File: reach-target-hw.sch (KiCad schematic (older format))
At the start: 53 parts, among them J1 CONN_01X02, J2 CONN_01X02, J3 CONN_02X05, J4 MODULE_HEADER, J5 MODULE_HEADER, J6 MODULE_HEADER, P1 CONN_01X05, P2 CONN_01X05, P3 CONN_01X02, P4 CONN_01X02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

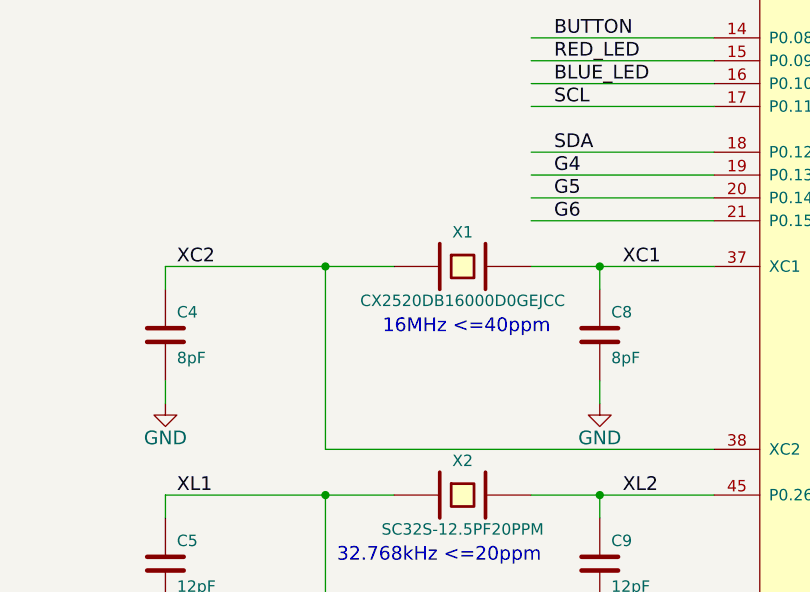
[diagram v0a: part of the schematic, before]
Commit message: symbol swap for 4pin xtal
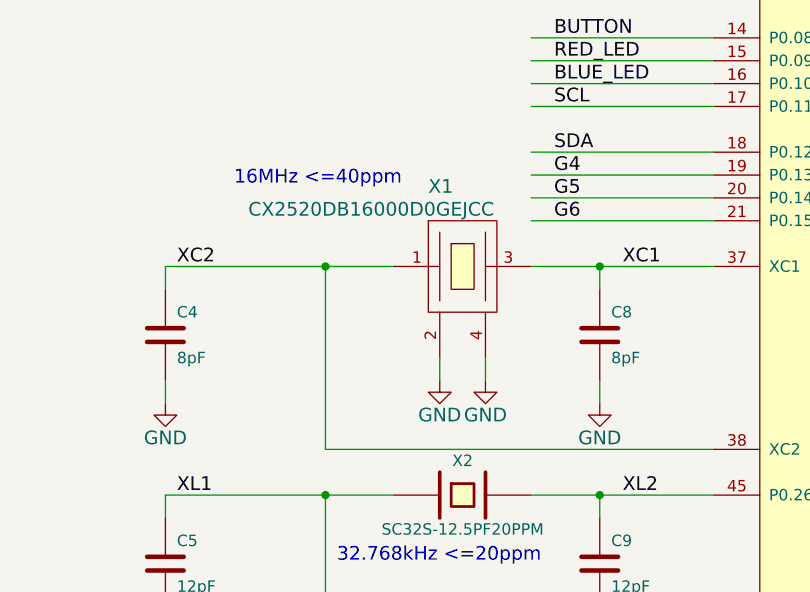
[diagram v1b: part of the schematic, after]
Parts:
- removed X1: CX2520DB16000D0GEJCC, !Parts:CX2520DB, symbol CRYSTAL
- added X1: CX2520DB16000D0GEJCC, symbol CRYSTAL-4
- J5, J6: footprint !Parts:MODULE_HEADER_TESSEL -> Pin_Headers:Pin_Header_Straight_1x10
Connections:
- wire segments 216 -> 218

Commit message: forgot to connect the eeprom
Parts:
- added R10, R11: 0R DNP, !Parts:SMD-0402, symbol R
- X1: footprint (none) -> !Parts:CX2520DB
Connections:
- net labels added: ANT, ANT1, ANT2, BLED, PI, RLED, VDD_PA
- wire segments 218 -> 222
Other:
- moved on the sheet: U1

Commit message: preliminary placement, i2c pull resistors
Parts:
- added R? (x2): 10kR DNP, !Parts:SMD-0402, symbol R
- C2, C3: footprint !Parts:SMD-0603 -> !Parts:SMD-0402
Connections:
- wire segments 222 -> 266
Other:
- moved on the sheet: R10, R11, U1

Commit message: never thought fitting all the io breakout would be the hard part of this board...
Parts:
- gave numbers to parts that had none: 2
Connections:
- net labels added: SWDIO-~RESET
- wire segments 266 -> 226
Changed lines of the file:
@@
 $EndComp
 Text Label 6800 2900 0    60   ~ 0
-SWDIO/~RESET
+SWDIO-~RESET
 Text Label 6800 3000 0    60   ~ 0
 SWDCLK
@@
 $EndComp
 Text Label 9400 9000 2    60   ~ 0
-SWDIO/~RESET
+SWDIO-~RESET
 Text Label 9400 9100 2    60   ~ 0
 SWDCLK
@@
 	2900 2800 2900 2900
 Wire Wire Line
-	2200 2800 2300 2800
-Wire Wire Line
-	2300 2800 2900 2800
-Wire Wire Line
-	2900 2800 3100 2800
+	2200 2800 3100 2800
 Wire Wire Line
 	2600 2300 2600 2200
@@
 	2600 1700 2600 1800
 Wire Wire Line
-	1500 1700 1700 1700
-Wire Wire Line
-	1700 1700 2200 1700
-Wire Wire Line
-	2200 1700 2600 1700
-Wire Wire Line
-	2600 1700 3000 1700
+	1500 1700 3000 1700
 Wire Wire Line
 	3000 2400 3800 2400
@@
 	5300 2800 5200 2800
 Wire Wire Line
-	5300 2700 5300 2800
-Wire Wire Line
-	5300 2800 5300 3000
+	5300 2700 5300 3000
 Wire Wire Line
 	5200 2700 5300 2700
 Wire Wire Line
-	5200 2400 5600 2400
-Wire Wire Line
-	5600 2400 5700 2400
+	5200 2400 5700 2400
 Wire Wire Line
 	5700 2400 5700 2200
@@
 	12000 5100 12000 5200
 Wire Wire Line
-	11800 5100 12000 5100
-Wire Wire Line
-	12000 5100 12400 5100
+	11800 5100 12400 5100
 Connection ~ 11000 5100
 Wire Wire Line
@@
 	11000 5100 11000 5200
 Wire Wire Line
-	10800 5100 11000 5100
-Wire Wire Line
-	11000 5100 11200 5100
+	10800 5100 11200 5100
 Connection ~ 10200 5100
 Connection ~ 10100 6900
@@
 	10200 5100 10200 5200
 Wire Wire Line
-	9900 5100 10200 5100
-Wire Wire Line
-	10200 5100 10400 5100
-Wire Wire Line
-	10100 6800 10100 6900
-Wire Wire Line
-	10100 6900 10100 7000
+	9900 5100 10400 5100
+Wire Wire Line
+	10100 6800 10100 7000
 Wire Wire Line
 	9900 6900 10100 6900
@@
 	10200 6000 10200 5800
 Wire Wire Line
-	9900 6000 10100 6000
-Wire Wire Line
-	10100 6000 10200 6000
+	9900 6000 10200 6000
 Connection ~ 8800 2300
 Wire Wire Line
@@
 	8800 2300 8700 2300
 Wire Wire Line
-	8800 1400 8800 2300
-Wire Wire Line
-	8800 2300 8800 2400
+	8800 1400 8800 2400
 Wire Wire Line
 	11100 1400 11100 1600
@@
 	11800 2900 11800 3000
 Wire Wire Line
-	11700 2900 11800 2900
-Wire Wire Line
-	11800 2900 12600 2900
+	11700 2900 12600 2900
 Wire Wire Line
 	10700 2900 11100 2900
@@
 	5100 6200 5100 6300
 Wire Wire Line
-	5100 6200 5800 6200
-Wire Wire Line
-	5800 6200 6100 6200
+	5100 6200 6100 6200
 Wire Wire Line
 	5800 7000 5800 6200
@@
 	7000 6800 7000 6700
 Wire Wire Line
-	6700 6200 7000 6200
-Wire Wire Line
-	7000 6200 7500 6200
+	6700 6200 7500 6200
 Wire Wire Line
 	5100 5800 5100 5700
@@
 	5100 5200 5100 5300
 Wire Wire Line
-	5100 5200 5800 5200
-Wire Wire Line
-	5800 5200 6100 5200
+	5100 5200 6100 5200
 Wire Wire Line
 	5800 6000 5800 5200
@@
 	7000 5800 7000 5700
 Wire Wire Line
-	6700 5200 7000 5200
-Wire Wire Line
-	7000 5200 7500 5200
+	6700 5200 7500 5200
 Connection ~ 8400 2300
 Connection ~ 8500 2300
@@
 	8400 2300 8500 2300
 Wire Wire Line
-	8500 1450 8500 2300
-Wire Wire Line
-	8500 2300 8500 2400
+	8500 1450 8500 2400
 Wire Wire Line
 	6800 1450 8500 1450
 Wire Wire Line
-	6800 1150 6800 1450
-Wire Wire Line
-	6800 1450 6800 1600
+	6800 1150 6800 1600
 Wire Wire Line
 	6800 2100 6800 2000
@@
 	8400 1500 7600 1500
 Wire Wire Line
-	8400 1500 8400 2300
-Wire Wire Line
-	8400 2300 8400 2400
+	8400 1500 8400 2400
 Wire Wire Line
 	7600 2100 7600 2000
@@
 Connection ~ 8500 7500
 Wire Wire Line
-	8500 7500 8600 7500
-Wire Wire Line
-	8600 7500 8700 7500
-Wire Wire Line
-	8700 7500 8900 7500
+	8500 7500 8900 7500
 Wire Wire Line
 	8600 7400 8600 7500
 Wire Wire Line
-	8500 7400 8500 7500
-Wire Wire Line
-	8500 7500 8500 7600
+	8500 7400 8500 7600
 Wire Wire Line
 	3500 5200 2600 5200
 Wire Wire Line
-	3600 5300 3500 5300
-Wire Wire Line
-	3500 5300 2600 5300
+	2600 5300 3600 5300
 Wire Wire Line
 	3400 5500 2600 5500
@@
 	1700 7200 1700 7000
 Wire Wire Line
-	2400 7200 2600 7200
-Wire Wire Line
-	2600 7200 3000 7200
-Wire Wire Line
-	3000 7200 3700 7200
+	2400 7200 3700 7200
 Wire Wire Line
 	2600 7300 2600 7200
@@
 	7900 9000 9800 9000
 Wire Wire Line
-	7200 9100 7200 9200
-Wire Wire Line
-	7200 9200 7200 9500
+	7200 9100 7200 9500
 Wire Wire Line
 	7200 9200 7400 9200
@@
 	7400 9300 6700 9300
 Wire Wire Line
-	9800 8900 9800 9000
-Wire Wire Line
-	9800 9000 9800 9100
+	9800 8900 9800 9100
 Connection ~ 9800 9000
 Wire Wire Line
@@
 	1500 1800 1600 1800
 Wire Wire Line
-	1600 1800 1600 2400
-Wire Wire Line
-	1600 2400 1600 2600
+	1600 1800 1600 2600
 Wire Wire Line
 	1500 2400 1600 2400
@@
 	15100 6100 14700 6100
 Wire Wire Line
-	14700 6100 14700 6400
-Wire Wire Line
-	14700 6400 14700 7000
-Wire Wire Line
-	14700 7000 14700 7600
-Wire Wire Line
-	14700 7600 14700 8200
-Wire Wire Line
-	14700 8200 14700 8800
-Wire Wire Line
-	14700 8800 14700 9000
+	14700 6100 14700 9000
 Wire Wire Line
 	14800 8800 14700 8800
@@
 	15100 6200 14600 6200
 Wire Wire Line
-	14600 6000 14600 6200
-Wire Wire Line
-	14600 6200 14600 6500
-Wire Wire Line
-	14600 6500 14600 7100
-Wire Wire Line
-	14600 7100 14600 7700
-Wire Wire Line
-	14600 7700 14600 8300
-Wire Wire Line
-	14600 8300 14600 8900
+	14600 6000 14600 8900
 Wire Wire Line
 	14600 6500 14800 6500
@@
 RLED
 $Comp
-L R R?
+L R R13
 U 1 1 54D9731D
 P 4500 4750
-F 0 "R?" V 4580 4750 50  0000 C CNN
+F 0 "R13" V 4580 4750 50  0000 C CNN
 F 1 "10kR DNP" V 4507 4751 50  0000 C CNN
 F 2 "!Parts:SMD-0402" V 4430 4750 30  0001 C CNN
@@
 $EndComp
 $Comp
-L R R?
+L R R12
 U 1 1 54D975E9
 P 4200 4750
-F 0 "R?" V 4280 4750 50  0000 C CNN
+F 0 "R12" V 4280 4750 50  0000 C CNN
 F 1 "10kR DNP" V 4207 4751 50  0000 C CNN
 F 2 "!Parts:SMD-0402" V 4130 4750 30  0001 C CNN
@@
 	4200 5000 4200 5300
 $Comp
-L +3V3 #PWR?
+L +3V3 #PWR044
 U 1 1 54D977F4
 P 4500 4400
-F 0 "#PWR?" H 4500 4250 60  0001 C CNN
+F 0 "#PWR044" H 4500 4250 60  0001 C CNN
 F 1 "+3V3" H 4500 4540 60  0000 C CNN
 F 2 "" H 4500 4400 60  0000 C CNN
@@
 	4500 4500 4500 4400
 $Comp
-L +3V3 #PWR?
+L +3V3 #PWR045
 U 1 1 54D978E6
 P 4200 4400
-F 0 "#PWR?" H 4200 4250 60  0001 C CNN
+F 0 "#PWR045" H 4200 4250 60  0001 C CNN
 F 1 "+3V3" H 4200 4540 60  0000 C CNN
 F 2 "" H 4200 4400 60  0000 C CNN

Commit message: well there goes most of the layout...and the avdd return path :/
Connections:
- net labels removed: SWDIO/~RESET
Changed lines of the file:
@@
 $EndComp
 Text Label 9400 9400 2    60   ~ 0
-SWDIO/~RESET
+SWDIO-~RESET
 $Comp
 L R R7

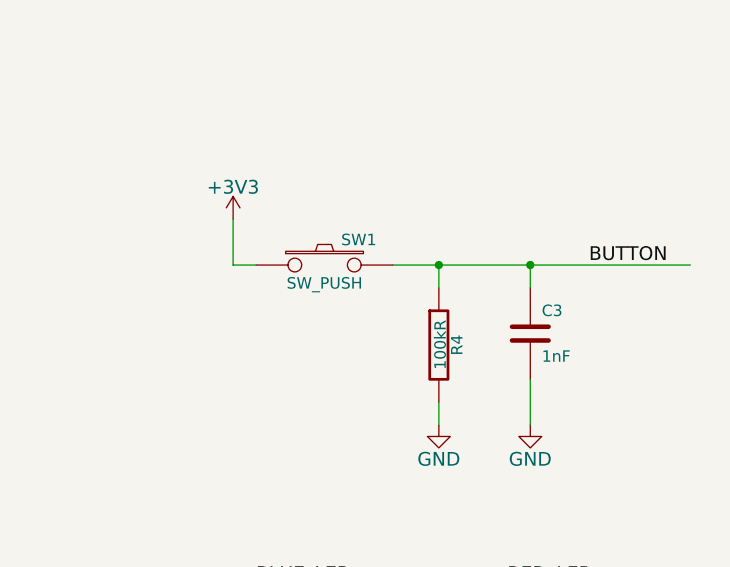
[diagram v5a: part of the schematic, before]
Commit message: swapped in real button
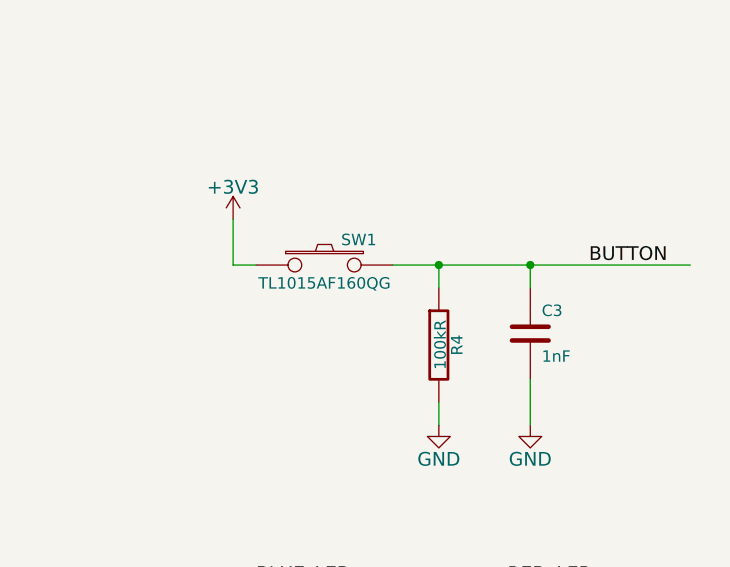
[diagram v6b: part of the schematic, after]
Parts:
- SW1: value SW_PUSH -> TL1015AF160QG; footprint Pin_Headers:Pin_Header_Straight_1x02 -> !Parts:TL1015AF160QG
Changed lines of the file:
@@
 P 2100 7200
 F 0 "SW1" H 2250 7310 50  0000 C CNN
-F 1 "SW_PUSH" H 2100 7120 50  0000 C CNN
-F 2 "Pin_Headers:Pin_Header_Straight_1x02" H 2100 7200 60  0001 C CNN
-F 3 "" H 2100 7200 60  0000 C CNN
+F 1 "TL1015AF160QG" H 2100 7120 50  0000 C CNN
+F 2 "!Parts:TL1015AF160QG" H 2100 7200 60  0001 C CNN
+F 3 "http://spec_sheets.e-switch.com/specs/P420000.pdf" H 2100 7200 60  0001 C CNN
 	1    2100 7200
 	1    0    0    -1

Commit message: better models
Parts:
- C1, C10, C17, C6: footprint !Parts:SMD-0603 -> !Parts:SMD-0603-C
- C11, C12, C13, C14, C15, C16, C18, C2, C3, C4, C5, C7, C8, C9: footprint !Parts:SMD-0402 -> !Parts:SMD-0402-C
- L1, L2, L4, L5, R1, R10, R11, R12, R13, R2, R3, R4, R5, R6, R7, R8, R9: footprint !Parts:SMD-0402 -> !Parts:SMD-0402-R
- L3: footprint !Parts:SMD-0603 -> !Parts:SMD-0603-R
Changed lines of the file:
@@
 F 0 "C10" H 7650 1900 50  0000 L CNN
 F 1 "4.7uF 10% X5R" H 7650 1700 50  0000 L CNN
-F 2 "!Parts:SMD-0603" H 7638 1650 30  0001 C CNN
+F 2 "!Parts:SMD-0603-C" H 7638 1650 30  0001 C CNN
 F 3 "" H 7600 1800 60  0000 C CNN
 	1    7600 1800
@@
 F 0 "L3" V 10350 2900 50  0000 C CNN
 F 1 "LBMF1608T100K" V 10500 2900 50  0000 C CNN
-F 2 "!Parts:SMD-0603" H 10400 2900 60  0001 C CNN
+F 2 "!Parts:SMD-0603-R" H 10400 2900 60  0001 C CNN
 F 3 "http://www.yuden.co.jp/ut/product/category/inductor/LBMF1608T100K.pdf" H 10400 2900 60  0001 C CNN
 	1    10400 2900
@@
 F 0 "C7" H 6850 1900 50  0000 L CNN
 F 1 "100nF 10% X7R" H 6850 1700 50  0000 L CNN
-F 2 "!Parts:SMD-0402" H 6838 1650 30  0001 C CNN
+F 2 "!Parts:SMD-0402-C" H 6838 1650 30  0001 C CNN
 F 3 "" H 6800 1800 60  0000 C CNN
 	1    6800 1800
@@
 F 0 "C8" H 7050 5600 50  0000 L CNN
 F 1 "8pF" H 7050 5400 50  0000 L CNN
-F 2 "!Parts:SMD-0402" H 7038 5350 30  0001 C CNN
+F 2 "!Parts:SMD-0402-C" H 7038 5350 30  0001 C CNN
 F 3 "" H 7000 5500 60  0000 C CNN
 	1    7000 5500
@@
 F 0 "L4" V 11350 2900 50  0000 C CNN
 F 1 "CW100505-15NJ" V 11500 2900 50  0000 C CNN
-F 2 "!Parts:SMD-0402" H 11400 2900 60  0001 C CNN
+F 2 "!Parts:SMD-0402-R" H 11400 2900 60  0001 C CNN
 F 3 "http://www.bourns.com/data/global/pdfs/CW100505.pdf" H 11400 2900 60  0001 C CNN
 	1    11400 2900
@@
 F 0 "C17" H 11850 3300 50  0000 L CNN
 F 1 "1.0uF 10% X7R" H 11850 3100 50  0000 L CNN
-F 2 "!Parts:SMD-0603" H 11838 3050 30  0001 C CNN
+F 2 "!Parts:SMD-0603-C" H 11838 3050 30  0001 C CNN
 F 3 "" H 11800 3200 60  0000 C CNN
 	1    11800 3200
@@
 F 0 "C4" H 5150 5600 50  0000 L CNN
 F 1 "8pF" H 5150 5400 50  0000 L CNN
-F 2 "!Parts:SMD-0402" H 5138 5350 30  0001 C CNN
+F 2 "!Parts:SMD-0402-C" H 5138 5350 30  0001 C CNN
 F 3 "" H 5100 5500 60  0000 C CNN
 	1    5100 5500
@@
 F 0 "C9" H 7050 6600 50  0000 L CNN
 F 1 "12pF" H 7050 6400 50  0000 L CNN
-F 2 "!Parts:SMD-0402" H 7038 6350 30  0001 C CNN
+F 2 "!Parts:SMD-0402-C" H 7038 6350 30  0001 C CNN
 F 3 "" H 7000 6500 60  0000 C CNN
 	1    7000 6500
@@
 F 0 "C5" H 5150 6600 50  0000 L CNN
 F 1 "12pF" H 5150 6400 50  0000 L CNN
-F 2 "!Parts:SMD-0402" H 5138 6350 30  0001 C CNN
+F 2 "!Parts:SMD-0402-C" H 5138 6350 30  0001 C CNN
 F 3 "" H 5100 6500 60  0000 C CNN
 	1    5100 6500
@@
 F 0 "C11" H 9550 1900 50  0000 L CNN
 F 1 "47nF 10% X7R" H 9550 1700 50  0000 L CNN
-F 2 "!Parts:SMD-0402" H 9538 1650 30  0001 C CNN
+F 2 "!Parts:SMD-0402-C" H 9538 1650 30  0001 C CNN
 F 3 "" H 9500 1800 60  0000 C CNN
 	1    9500 1800
@@
 F 0 "C13" H 10350 1900 50  0000 L CNN
 F 1 "100nF 10% X7R" H 10350 1700 50  0000 L CNN
-F 2 "!Parts:SMD-0402" H 10338 1650 30  0001 C CNN
+F 2 "!Parts:SMD-0402-C" H 10338 1650 30  0001 C CNN
 F 3 "" H 10300 1800 60  0000 C CNN
 	1    10300 1800
@@
 F 0 "C16" H 11150 1900 50  0000 L CNN
 F 1 "1nF 10% X7R" H 11150 1700 50  0000 L CNN
-F 2 "!Parts:SMD-0402" H 11138 1650 30  0001 C CNN
+F 2 "!Parts:SMD-0402-C" H 11138 1650 30  0001 C CNN
 F 3 "" H 11100 1800 60  0000 C CNN
 	1    11100 1800
@@
 F 0 "L2" V 10150 5500 50  0000 C CNN
 F 1 "4.7nH 5% HF" V 10300 5500 50  0000 C CNN
-F 2 "!Parts:SMD-0402" H 10200 5500 60  0001 C CNN
+F 2 "!Parts:SMD-0402-R" H 10200 5500 60  0001 C CNN
 F 3 "" H 10200 5500 60  0000 C CNN
 	1    10200 5500
@@
 F 0 "L1" V 10050 6500 50  0000 C CNN
 F 1 "10nH 5% HF" V 10200 6500 50  0000 C CNN
-F 2 "!Parts:SMD-0402" H 10100 6500 60  0001 C CNN
+F 2 "!Parts:SMD-0402-R" H 10100 6500 60  0001 C CNN
 F 3 "" H 10100 6500 60  0000 C CNN
 	1    10100 6500
@@
 F 0 "C12" H 10150 7300 50  0000 L CNN
 F 1 "2.2nF" H 10150 7100 50  0000 L CNN
-F 2 "!Parts:SMD-0402" H 10138 7050 30  0001 C CNN
+F 2 "!Parts:SMD-0402-C" H 10138 7050 30  0001 C CNN
 F 3 "" H 10100 7200 60  0000 C CNN
 	1    10100 7200
@@
 F 0 "C14" H 10650 5200 50  0000 L CNN
 F 1 "2.2pF +/-0.1pF NPO" H 10650 5000 50  0000 L CNN
-F 2 "!Parts:SMD-0402" H 10638 4950 30  0001 C CNN
+F 2 "!Parts:SMD-0402-C" H 10638 4950 30  0001 C CNN
 F 3 "" H 10600 5100 60  0000 C CNN
 	1    10600 5100
@@
 F 0 "C15" H 11050 5500 50  0000 L CNN
 F 1 "1pF +/-0.1pF NPO" H 11050 5300 50  0000 L CNN
-F 2 "!Parts:SMD-0402" H 11038 5250 30  0001 C CNN
+F 2 "!Parts:SMD-0402-C" H 11038 5250 30  0001 C CNN
 F 3 "" H 11000 5400 60  0000 C CNN
 	1    11000 5400
@@
 F 0 "L5" V 11450 5100 50  0000 C CNN
 F 1 "3.3nH 5% HF" V 11600 5100 50  0000 C CNN
-F 2 "!Parts:SMD-0402" H 11500 5100 60  0001 C CNN
+F 2 "!Parts:SMD-0402-R" H 11500 5100 60  0001 C CNN
 F 3 "" H 11500 5100 60  0000 C CNN
 	1    11500 5100
@@
 F 0 "C18" H 12050 5500 50  0000 L CNN
 F 1 "1.5pF +/-0.1pF NPO" H 12050 5300 50  0000 L CNN
-F 2 "!Parts:SMD-0402" H 12038 5250 30  0001 C CNN
+F 2 "!Parts:SMD-0402-C" H 12038 5250 30  0001 C CNN
 F 3 "" H 12000 5400 60  0000 C CNN
 	1    12000 5400
@@
 F 0 "R2" V 2380 3150 50  0000 C CNN
 F 1 "100kR 1%" V 2307 3151 50  0000 C CNN
-F 2 "!Parts:SMD-0402" V 2230 3150 30  0001 C CNN
+F 2 "!Parts:SMD-0402-R" V 2230 3150 30  0001 C CNN
 F 3 "" H 2300 3150 30  0000 C CNN
 	1    2300 3150
@@
 F 0 "R1" V 2280 2450 50  0000 C CNN
 F 1 "619kR 1%" V 2207 2451 50  0000 C CNN
-F 2 "!Parts:SMD-0402" V 2130 2450 30  0001 C CNN
+F 2 "!Parts:SMD-0402-R" V 2130 2450 30  0001 C CNN
 F 3 "" H 2200 2450 30  0000 C CNN
 	1    2200 2450
@@
 F 0 "C1" H 2650 2100 50  0000 L CNN
 F 1 "4.7uF" H 2650 1900 50  0000 L CNN
-F 2 "!Parts:SMD-0603" H 2638 1850 30  0001 C CNN
+F 2 "!Parts:SMD-0603-C" H 2638 1850 30  0001 C CNN
 F 3 "" H 2600 2000 60  0000 C CNN
 	1    2600 2000
@@
 F 0 "C6" H 5650 2800 50  0000 L CNN
 F 1 "4.7uF" H 5650 2600 50  0000 L CNN
-F 2 "!Parts:SMD-0603" H 5638 2550 30  0001 C CNN
+F 2 "!Parts:SMD-0603-C" H 5638 2550 30  0001 C CNN
 F 3 "" H 5600 2700 60  0000 C CNN
 	1    5600 2700
@@
 F 0 "C2" H 2950 3200 50  0000 L CNN
 F 1 "100nF" H 2950 3000 50  0000 L CNN
-F 2 "!Parts:SMD-0402" H 2938 2950 30  0001 C CNN
+F 2 "!Parts:SMD-0402-C" H 2938 2950 30  0001 C CNN
 F 3 "" H 2900 3100 60  0000 C CNN
 	1    2900 3100
@@
 F 0 "R4" V 2680 7550 50  0000 C CNN
 F 1 "100kR" V 2607 7551 50  0000 C CNN
-F 2 "!Parts:SMD-0402" V 2530 7550 30  0001 C CNN
+F 2 "!Parts:SMD-0402-R" V 2530 7550 30  0001 C CNN
 F 3 "" H 2600 7550 30  0000 C CNN
 	1    2600 7550
@@
 F 0 "C3" H 3050 7600 50  0000 L CNN
 F 1 "1nF" H 3050 7400 50  0000 L CNN
-F 2 "!Parts:SMD-0402" H 3038 7350 30  0001 C CNN
+F 2 "!Parts:SMD-0402-C" H 3038 7350 30  0001 C CNN
 F 3 "" H 3000 7500 60  0000 C CNN
 	1    3000 7500
@@
 F 0 "R3" V 2480 9450 50  0000 C CNN
 F 1 "1kR" V 2407 9451 50  0000 C CNN
-F 2 "!Parts:SMD-0402" V 2330 9450 30  0001 C CNN
+F 2 "!Parts:SMD-0402-R" V 2330 9450 30  0001 C CNN
 F 3 "" H 2400 9450 30  0000 C CNN
 	1    2400 9450
@@
 F 0 "R6" V 3580 9450 50  0000 C CNN
 F 1 "1kR" V 3507 9451 50  0000 C CNN
-F 2 "!Parts:SMD-0402" V 3430 9450 30  0001 C CNN
+F 2 "!Parts:SMD-0402-R" V 3430 9450 30  0001 C CNN
 F 3 "" H 3500 9450 30  0000 C CNN
 	1    3500 9450
@@
 F 0 "R7" V 8530 9400 50  0000 C CNN
 F 1 "0R DNP" V 8457 9401 50  0000 C CNN
-F 2 "!Parts:SMD-0402" V 8380 9400 30  0001 C CNN
+F 2 "!Parts:SMD-0402-R" V 8380 9400 30  0001 C CNN
 F 3 "" H 8450 9400 30  0000 C CNN
 	1    8450 9400
@@
 F 0 "R9" V 9880 9350 50  0000 C CNN
 F 1 "10kR DNP" V 9807 9351 50  0000 C CNN
-F 2 "!Parts:SMD-0402" V 9730 9350 30  0001 C CNN
+F 2 "!Parts:SMD-0402-R" V 9730 9350 30  0001 C CNN
 F 3 "" H 9800 9350 30  0000 C CNN
 	1    9800 9350
@@
 F 0 "R8" V 9880 8650 50  0000 C CNN
 F 1 "10kR DNP" V 9807 8651 50  0000 C CNN
-F 2 "!Parts:SMD-0402" V 9730 8650 30  0001 C CNN
+F 2 "!Parts:SMD-0402-R" V 9730 8650 30  0001 C CNN
 F 3 "" H 9800 8650 30  0000 C CNN
 	1    9800 8650
@@
 F 0 "R5" V 3430 2800 50  0000 C CNN
 F 1 "1kR" V 3357 2801 50  0000 C CNN
-F 2 "!Parts:SMD-0402" V 3280 2800 30  0001 C CNN
+F 2 "!Parts:SMD-0402-R" V 3280 2800 30  0001 C CNN
 F 3 "" H 3350 2800 30  0000 C CNN
 	1    3350 2800
@@
 F 0 "R10" V 3930 5100 50  0000 C CNN
 F 1 "0R DNP" V 3857 5101 50  0000 C CNN
-F 2 "!Parts:SMD-0402" V 3780 5100 30  0001 C CNN
+F 2 "!Parts:SMD-0402-R" V 3780 5100 30  0001 C CNN
 F 3 "" H 3850 5100 30  0000 C CNN
 	1    3850 5100
@@
 F 0 "R11" V 3930 5300 50  0000 C CNN
 F 1 "0R DNP" V 3857 5301 50  0000 C CNN
-F 2 "!Parts:SMD-0402" V 3780 5300 30  0001 C CNN
+F 2 "!Parts:SMD-0402-R" V 3780 5300 30  0001 C CNN
 F 3 "" H 3850 5300 30  0000 C CNN
 	1    3850 5300
@@
 F 0 "R13" V 4580 4750 50  0000 C CNN
 F 1 "10kR DNP" V 4507 4751 50  0000 C CNN
-F 2 "!Parts:SMD-0402" V 4430 4750 30  0001 C CNN
+F 2 "!Parts:SMD-0402-R" V 4430 4750 30  0001 C CNN
 F 3 "" H 4500 4750 30  0000 C CNN
 	1    4500 4750
@@
 F 0 "R12" V 4280 4750 50  0000 C CNN
 F 1 "10kR DNP" V 4207 4751 50  0000 C CNN
-F 2 "!Parts:SMD-0402" V 4130 4750 30  0001 C CNN
+F 2 "!Parts:SMD-0402-R" V 4130 4750 30  0001 C CNN
 F 3 "" H 4200 4750 30  0000 C CNN
 	1    4200 4750
